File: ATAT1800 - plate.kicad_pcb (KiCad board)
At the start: 2 copper layers, 395 x 122.5 mm, 101 parts, among them SW1 MX_SW_solder, SW10 MX_SW_solder, SW100 MX_SW_solder, SW101 MX_SW_solder, SW11 MX_SW_solder, SW12 MX_SW_solder, SW13 MX_SW_solder, SW14 MX_SW_solder, SW15 MX_SW_solder, SW16 MX_SW_solder, SW17 MX_SW_solder, SW18 MX_SW_solder, SW19 MX_SW_solder, SW2 MX_SW_solder, SW20 MX_SW_solder, SW21 MX_SW_solder, SW22 MX_SW_solder, SW23 MX_SW_solder, SW24 MX_SW_solder, SW25 MX_SW_solder, SW26 MX_SW_solder, SW27 MX_SW_solder, SW28 MX_SW_solder, SW29 MX_SW_solder, SW3 MX_SW_solder, SW30 MX_SW_solder, SW31 MX_SW_solder, SW33 MX_SW_solder, SW34 MX_SW_solder, SW35 MX_SW_solder, SW36 MX_SW_solder, SW37 MX_SW_solder, SW38 MX_SW_solder, SW39 MX_SW_solder, SW4 MX_SW_solder, SW40 MX_SW_solder, SW41 MX_SW_solder, SW42 MX_SW_solder, SW43 MX_SW_solder, SW44 MX_SW_solder, SW45 MX_SW_solder, SW46 MX_SW_solder, SW47 MX_SW_solder, SW48 MX_SW_solder, SW49 MX_SW_solder, SW5 MX_SW_solder, SW50 MX_SW_solder, SW51 MX_SW_solder, SW52 MX_SW_solder, SW53 MX_SW_solder, SW54 MX_SW_solder, SW55 MX_SW_solder, SW57 MX_SW_solder, SW58 MX_SW_solder, SW59 MX_SW_solder, SW6 MX_SW_solder, SW60 MX_SW_solder, SW61 MX_SW_solder, SW62 MX_SW_solder, SW63 MX_SW_solder, SW64 MX_SW_solder, SW65 MX_SW_solder, SW66 MX_SW_solder, SW67 MX_SW_solder, SW68 MX_SW_solder, SW7 MX_SW_solder, SW70 MX_SW_solder, SW71 MX_SW_solder, SW72 MX_SW_solder, SW74 MX_SW_solder, SW75 MX_SW_solder, SW76 MX_SW_solder, SW77 MX_SW_solder, SW78 MX_SW_solder, SW79 MX_SW_solder, SW8 MX_SW_solder, SW80 MX_SW_solder, SW81 MX_SW_solder, SW82 MX_SW_solder, SW83 MX_SW_solder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

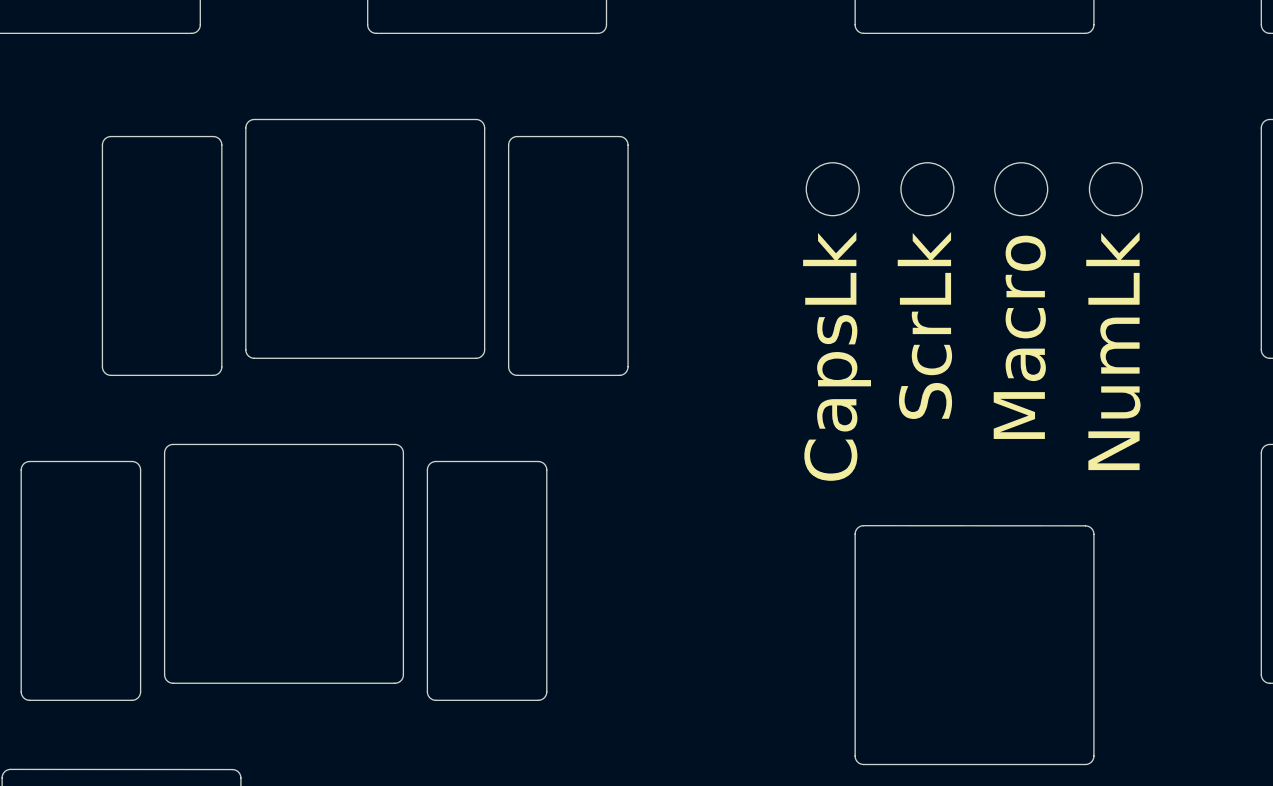
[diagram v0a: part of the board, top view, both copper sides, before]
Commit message: add mounting points. fix stab collision
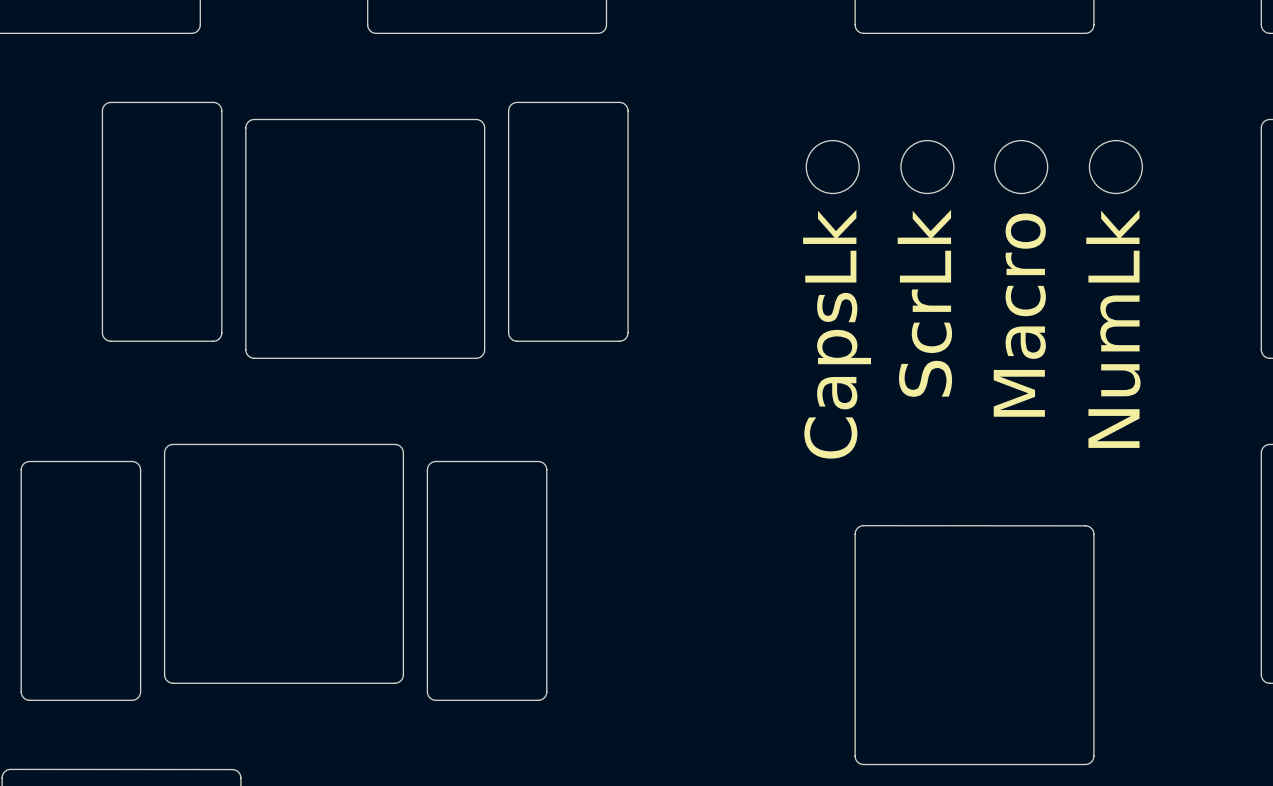
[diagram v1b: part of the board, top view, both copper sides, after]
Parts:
- turned S4 to 180 degrees
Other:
- outline, holes or cut-outs redrawn
